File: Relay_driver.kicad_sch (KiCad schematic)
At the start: 48 parts, among them U13 ULN2003A, U14 ULN2003A, U15 ULN2003A, U16 ULN2003A, U17 ULN2003A, U18 ULN2003A

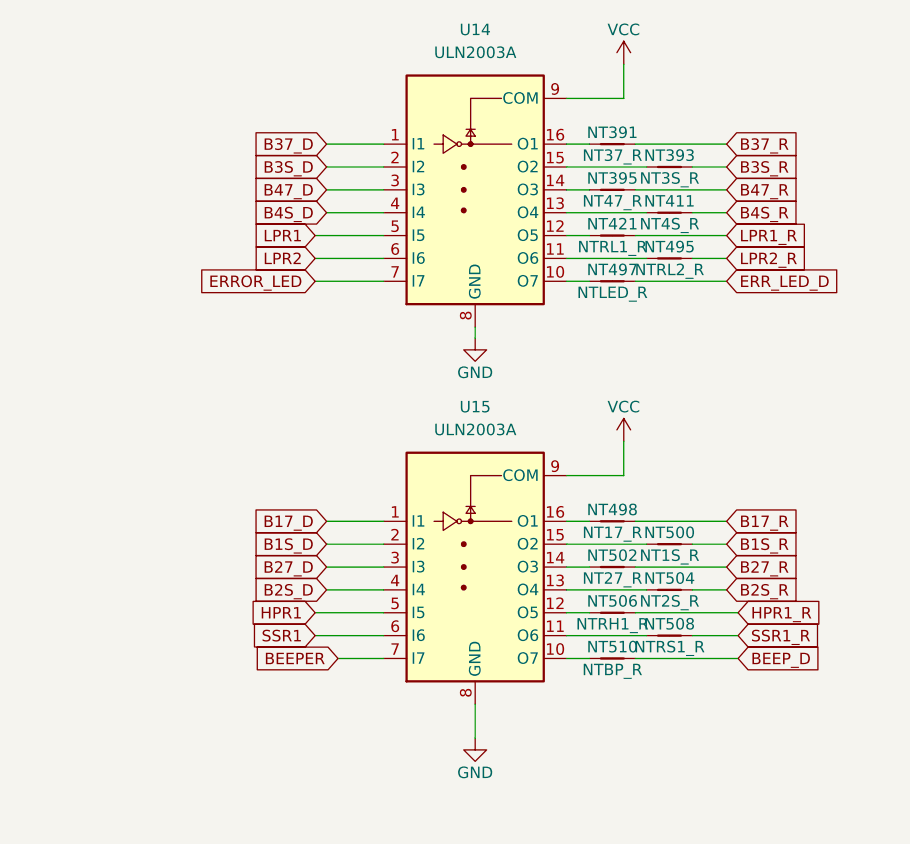
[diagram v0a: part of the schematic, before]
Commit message: half PCB completed
FTS io controller PCB
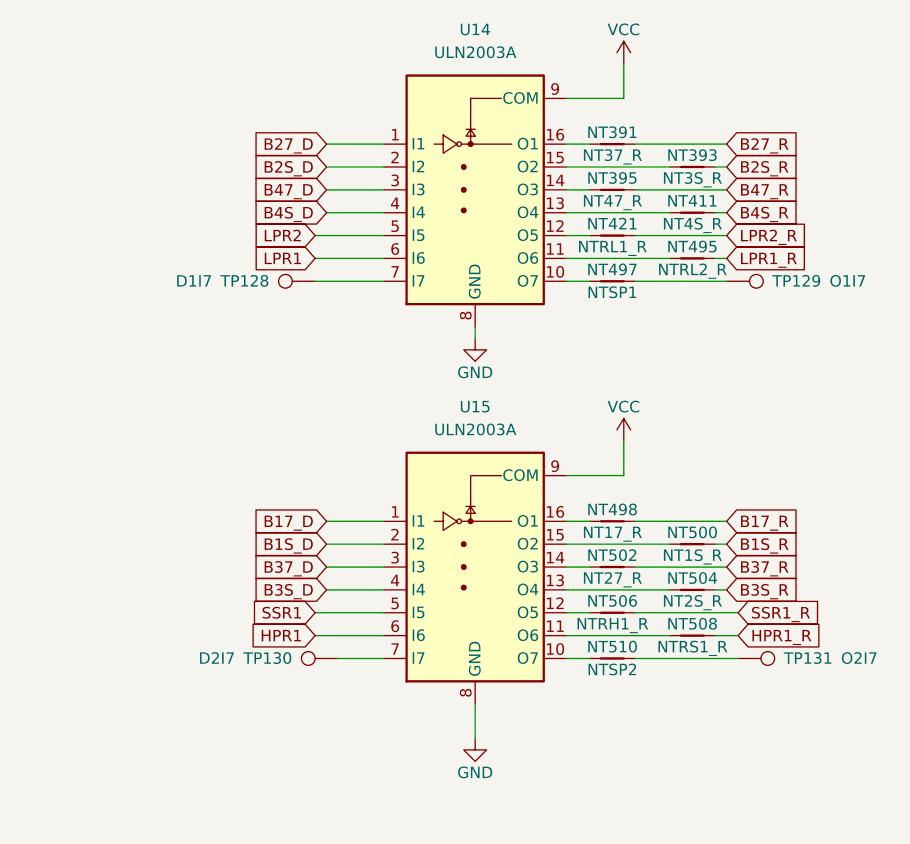
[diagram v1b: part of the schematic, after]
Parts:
- added TP128: D1I7, Connector_Pin:Pin_D0.9mm_L10.0mm_W2.4mm_FlatFork, symbol Connector:TestPoint
- added TP129: O1I7, Connector_Pin:Pin_D0.9mm_L10.0mm_W2.4mm_FlatFork, symbol Connector:TestPoint
- added TP130: D2I7, Connector_Pin:Pin_D0.9mm_L10.0mm_W2.4mm_FlatFork, symbol Connector:TestPoint
- added TP131: O2I7, Connector_Pin:Pin_D0.9mm_L10.0mm_W2.4mm_FlatFork, symbol Connector:TestPoint
- NT497: value NTLED_R -> NTSP1
- NT510: value NTBP_R -> NTSP2
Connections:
- net B27_D: now also U14.1 (I1); no longer U15.3 (I3)
- net B27_R: now also NT391.2; no longer NT502.2
- net B2S_D: now also U14.2 (I2); no longer U15.4 (I4)
- net B2S_R: now also NT393.2; no longer NT504.2
- net B37_D: now also U15.3 (I3); no longer U14.1 (I1)
- net B37_R: now also NT502.2; no longer NT391.2
- net B3S_D: now also U15.4 (I4); no longer U14.2 (I2)
- net B3S_R: now also NT504.2; no longer NT393.2
- net HPR1: now also U15.6 (I6); no longer U15.5 (I5)
- net HPR1_R: now also NT508.2; no longer NT506.2
- net LPR1: now also U14.6 (I6); no longer U14.5 (I5)
- net LPR1_R: now also NT495.2; no longer NT421.2
- net LPR2: now also U14.5 (I5); no longer U14.6 (I6)
- net LPR2_R: now also NT421.2; no longer NT495.2
- net SSR1: now also U15.5 (I5); no longer U15.6 (I6)
- net SSR1_R: now also NT506.2; no longer NT508.2
- net BEEPER: no longer names the net of U15.7 (I7)
- net BEEPER: now also TP130.1
- net BEEP_D: no longer names the net of NT510.2
- net BEEP_D: now also TP131.1
- net ERROR_LED: no longer names the net of U14.7 (I7)
- net ERROR_LED: now also TP128.1
- net ERR_LED_D: no longer names the net of NT497.2
- net ERR_LED_D: now also TP129.1
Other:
- moved on the sheet: NT393, NT411, NT495, NT500, NT504, NT508

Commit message: PCB Completed
PCB completed but final verification not completed
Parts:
- TP128, TP129, TP130, TP131: footprint Connector_Pin:Pin_D0.9mm_L10.0mm_W2.4mm_FlatFork -> TestPoint:TestPoint_THTPad_D1.5mm_Drill0.7mm
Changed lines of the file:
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@@
       (effects (font (size 1.27 1.27)) (justify left))
     )
-    (property "Footprint" "Connector_Pin:Pin_D0.9mm_L10.0mm_W2.4mm_FlatFork" (id 2) (at 129.54 40.64 0)
+    (property "Footprint" "TestPoint:TestPoint_THTPad_D1.5mm_Drill0.7mm" (id 2) (at 129.54 40.64 0)
       (effects (font (size 1.27 1.27)) hide)
     )
@@
       (effects (font (size 1.27 1.27)) (justify left))
     )
-    (property "Footprint" "Connector_Pin:Pin_D0.9mm_L10.0mm_W2.4mm_FlatFork" (id 2) (at 176.53 92.71 0)
+    (property "Footprint" "TestPoint:TestPoint_THTPad_D1.5mm_Drill0.7mm" (id 2) (at 176.53 92.71 0)
       (effects (font (size 1.27 1.27)) hide)
     )
@@
       (effects (font (size 1.27 1.27)) (justify left))
     )
-    (property "Footprint" "Connector_Pin:Pin_D0.9mm_L10.0mm_W2.4mm_FlatFork" (id 2) (at 132.08 82.55 0)
+    (property "Footprint" "TestPoint:TestPoint_THTPad_D1.5mm_Drill0.7mm" (id 2) (at 132.08 82.55 0)
       (effects (font (size 1.27 1.27)) hide)
     )
@@
       (effects (font (size 1.27 1.27)) (justify left))
     )
-    (property "Footprint" "Connector_Pin:Pin_D0.9mm_L10.0mm_W2.4mm_FlatFork" (id 2) (at 175.26 50.8 0)
-      (effects (font (size 1.27 1.27)) hide)
-    )
+    (property "Footprint" "TestPoint:TestPoint_THTPad_D1.5mm_Drill0.7mm" (id 2) (at 175.26 50.8 0)
+      (effects (font (size 1.27 1.27)) hide)
+    )
